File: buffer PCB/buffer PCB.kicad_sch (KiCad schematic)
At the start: 24 parts, among them J1 Conn_02x10_Odd_Even, J2 Conn_01x09, J3 Conn_01x09, J4 Conn_02x10_Odd_Even, U1 74HC245, U2 74HC245

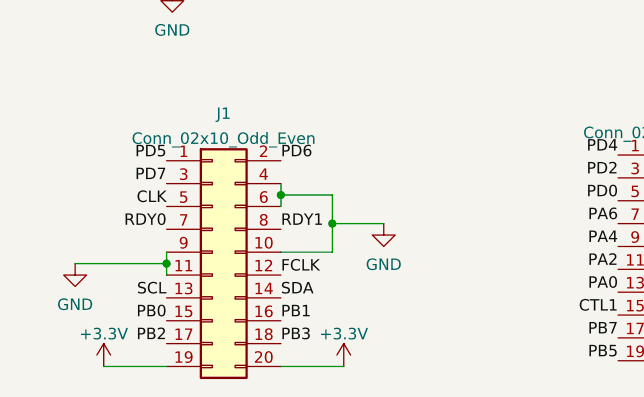
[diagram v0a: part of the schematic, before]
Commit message: updated for different board power pinout and proper hole locations
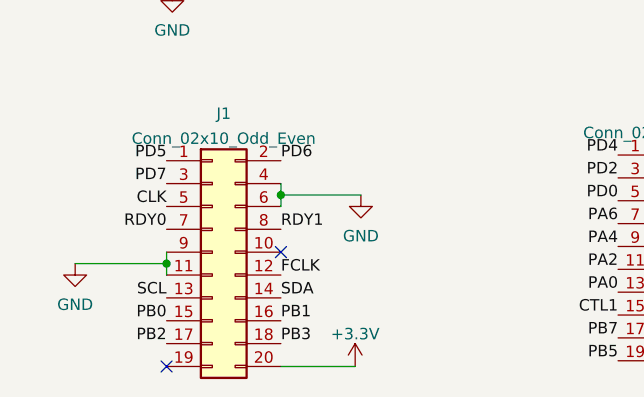
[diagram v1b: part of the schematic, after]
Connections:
- net +3V3: no longer J1.19 (Pin_19)
- net GND: no longer J1.10 (Pin_10)
- no-connect marks 0 -> 2
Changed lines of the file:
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@@
 (kicad_sch (version 20211123) (generator eeschema)
   (paper "A4")
-  (junction (at 113.03 115.57) (diameter 0) (color 0 0 0 0)
-  )
   (junction (at 82.55 81.915) (diameter 0) (color 0 0 0 0)
   )
@@
   (junction (at 107.315 112.395) (diameter 0) (color 0 0 0 0)
   )
-  (wire (pts (xy 87.63 131.445) (xy 94.615 131.445))
-    (stroke (width 0) (type default) (color 0 0 0 0))
-  )
+  (no_connect (at 107.315 118.745))
+  (no_connect (at 94.615 131.445))
   (wire (pts (xy 107.315 112.395) (xy 107.315 113.665))
     (stroke (width 0) (type default) (color 0 0 0 0))
@@
     (stroke (width 0) (type default) (color 0 0 0 0))
   )
-  (wire (pts (xy 113.03 112.395) (xy 113.03 115.57))
+  (wire (pts (xy 107.315 112.395) (xy 116.205 112.395))
     (stroke (width 0) (type default) (color 0 0 0 0))
   )
-  (wire (pts (xy 113.03 118.745) (xy 107.315 118.745))
-    (stroke (width 0) (type default) (color 0 0 0 0))
-  )
-  (wire (pts (xy 113.03 115.57) (xy 113.03 118.745))
-    (stroke (width 0) (type default) (color 0 0 0 0))
-  )
-  (wire (pts (xy 113.03 115.57) (xy 118.745 115.57))
-    (stroke (width 0) (type default) (color 0 0 0 0))
-  )
-  (wire (pts (xy 107.315 112.395) (xy 113.03 112.395))
-    (stroke (width 0) (type default) (color 0 0 0 0))
-  )
-  (wire (pts (xy 107.315 131.445) (xy 114.3 131.445))
+  (wire (pts (xy 107.315 131.445) (xy 115.57 131.445))
     (stroke (width 0) (type default) (color 0 0 0 0))
   )
@@
     (pin "1")
   )
-  (symbol (lib_id "power:+3.3V") (at 114.3 131.445 0) (unit 1)
-    (in_bom yes) (on_board yes) (fields_autoplaced)
-    (property "Reference" "#PWR08" (id 0) (at 114.3 135.255 0)
-      (effects (font (size 1.27 1.27)) hide)
-    )
-    (property "Value" "+3.3V" (id 1) (at 114.3 127.8405 0))
-    (property "Footprint" "" (id 2) (at 114.3 131.445 0)
-      (effects (font (size 1.27 1.27)) hide)
-    )
-    (property "Datasheet" "" (id 3) (at 114.3 131.445 0)
+  (symbol (lib_id "power:+3.3V") (at 115.57 131.445 0) (unit 1)
+    (in_bom yes) (on_board yes) (fields_autoplaced)
+    (property "Reference" "#PWR08" (id 0) (at 115.57 135.255 0)
+      (effects (font (size 1.27 1.27)) hide)
+    )
+    (property "Value" "+3.3V" (id 1) (at 115.57 127.8405 0))
+    (property "Footprint" "" (id 2) (at 115.57 131.445 0)
+      (effects (font (size 1.27 1.27)) hide)
+    )
+    (property "Datasheet" "" (id 3) (at 115.57 131.445 0)
       (effects (font (size 1.27 1.27)) hide)
     )
@@
     (pin "9")
   )
-  (symbol (lib_id "power:GND") (at 118.745 115.57 0) (unit 1)
-    (in_bom yes) (on_board yes) (fields_autoplaced)
-    (property "Reference" "#PWR010" (id 0) (at 118.745 121.92 0)
-      (effects (font (size 1.27 1.27)) hide)
-    )
-    (property "Value" "GND" (id 1) (at 118.745 120.1325 0))
-    (property "Footprint" "" (id 2) (at 118.745 115.57 0)
-      (effects (font (size 1.27 1.27)) hide)
-    )
-    (property "Datasheet" "" (id 3) (at 118.745 115.57 0)
+  (symbol (lib_id "power:GND") (at 116.205 112.395 0) (unit 1)
+    (in_bom yes) (on_board yes) (fields_autoplaced)
+    (property "Reference" "#PWR010" (id 0) (at 116.205 118.745 0)
+      (effects (font (size 1.27 1.27)) hide)
+    )
+    (property "Value" "GND" (id 1) (at 116.205 116.9575 0))
+    (property "Footprint" "" (id 2) (at 116.205 112.395 0)
+      (effects (font (size 1.27 1.27)) hide)
+    )
+    (property "Datasheet" "" (id 3) (at 116.205 112.395 0)
       (effects (font (size 1.27 1.27)) hide)
     )
@@
     (pin "1")
     (pin "2")
-  )
-  (symbol (lib_id "power:+3.3V") (at 87.63 131.445 0) (unit 1)
-    (in_bom yes) (on_board yes) (fields_autoplaced)
-    (property "Reference" "#PWR03" (id 0) (at 87.63 135.255 0)
-      (effects (font (size 1.27 1.27)) hide)
-    )
-    (property "Value" "+3.3V" (id 1) (at 87.63 127.8405 0))
-    (property "Footprint" "" (id 2) (at 87.63 131.445 0)
-      (effects (font (size 1.27 1.27)) hide)
-    )
-    (property "Datasheet" "" (id 3) (at 87.63 131.445 0)
-      (effects (font (size 1.27 1.27)) hide)
-    )
-    (pin "1")
   )
   (symbol (lib_id "Connector_Generic:Conn_02x10_Odd_Even") (at 149.86 118.11 0) (unit 1)
@@
       (reference "#PWR02") (unit 1) (value "GND") (footprint "")
     )
-    (path "/f4796b8f-ea14-46be-8925-224c0e07b391"
-      (reference "#PWR03") (unit 1) (value "+3.3V") (footprint "")
-    )
     (path "/dcf8af08-9c45-40ca-83b2-12a1e777375a"
